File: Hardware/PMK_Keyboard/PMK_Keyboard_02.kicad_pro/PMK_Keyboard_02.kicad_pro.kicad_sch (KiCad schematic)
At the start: 0 parts

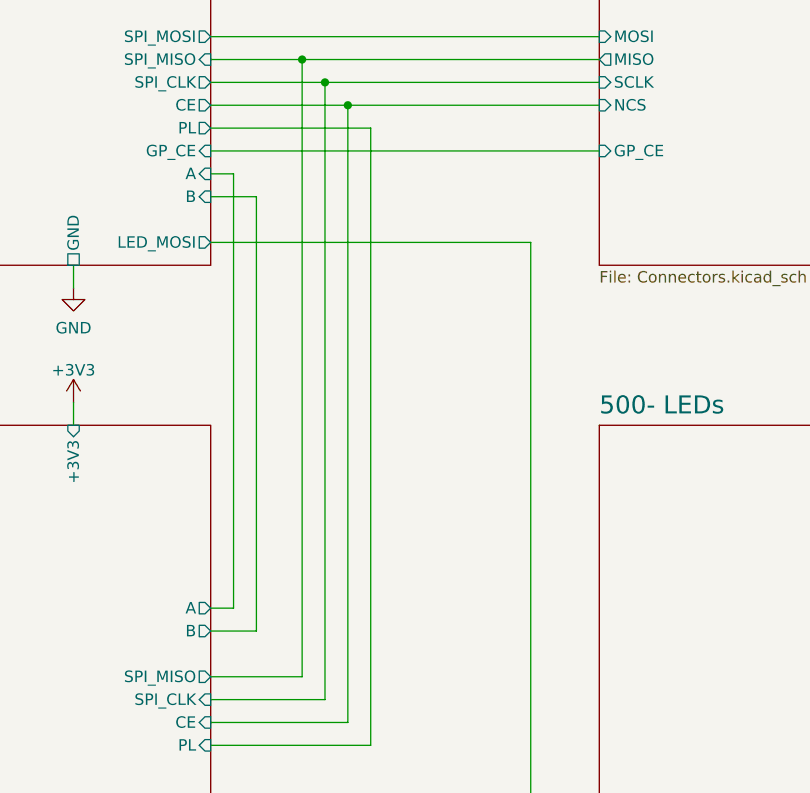
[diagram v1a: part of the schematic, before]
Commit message: added module connector
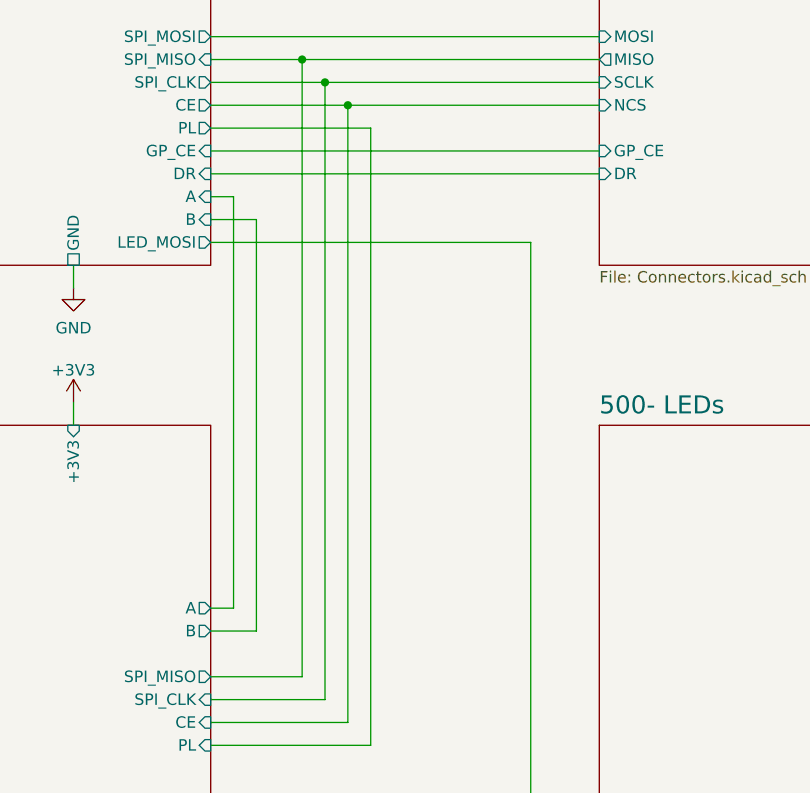
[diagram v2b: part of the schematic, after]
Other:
- sheet 200- PSoM ports: added DR; removed none
- sheet 300- Connectors ports: added DR; removed none
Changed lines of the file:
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@@
 	(wire
 		(pts
-			(xy 124.46 124.46) (xy 124.46 76.2)
+			(xy 124.46 124.46) (xy 124.46 78.74)
 		)
 		(stroke
@@
 	(wire
 		(pts
-			(xy 119.38 73.66) (xy 121.92 73.66)
+			(xy 119.38 76.2) (xy 121.92 76.2)
 		)
 		(stroke
@@
 	(wire
 		(pts
-			(xy 121.92 73.66) (xy 121.92 121.92)
+			(xy 121.92 76.2) (xy 121.92 121.92)
 		)
 		(stroke
@@
 	(wire
 		(pts
+			(xy 119.38 73.66) (xy 162.56 73.66)
+		)
+		(stroke
+			(width 0)
+			(type default)
+		)
+	)
+	(wire
+		(pts
 			(xy 215.9 30.48) (xy 215.9 33.02)
 		)
@@
 	(wire
 		(pts
-			(xy 124.46 76.2) (xy 119.38 76.2)
+			(xy 124.46 78.74) (xy 119.38 78.74)
 		)
 		(stroke
@@
 			)
 		)
+		(pin "DR" input
+			(at 162.56 73.66 180)
+			(effects
+				(font
+					(size 1.27 1.27)
+				)
+				(justify left)
+			)
+		)
 		(instances
 			(project "PMK_Keyboard_02.kicad_pro"
@@
 		)
 		(pin "B" input
+			(at 119.38 78.74 0)
+			(effects
+				(font
+					(size 1.27 1.27)
+				)
+				(justify right)
+			)
+		)
+		(pin "A" input
 			(at 119.38 76.2 0)
-			(effects
-				(font
-					(size 1.27 1.27)
-				)
-				(justify right)
-			)
-		)
-		(pin "A" input
-			(at 119.38 73.66 0)
 			(effects
 				(font
@@
 			(effects
 				(font
+					(size 1.27 1.27)
+				)
+				(justify right)
+			)
+		)
+		(pin "DR" input
+			(at 119.38 73.66 0)
+			(effects
+				(font

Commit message: working on routing
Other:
- sheet 400- Shift Register - Switch ports: added DB_A, DB_B; removed A, B
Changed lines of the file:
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@@
 			)
 		)
-		(pin "B" output
-			(at 119.38 124.46 0)
+		(pin "DB_A" output
+			(at 119.38 121.92 0)
 			(effects
 				(font
@@
 			)
 		)
-		(pin "A" output
-			(at 119.38 121.92 0)
+		(pin "DB_B" output
+			(at 119.38 124.46 0)
 			(effects
 				(font

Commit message: routing ongoing
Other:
- sheet 200- PSoM ports: added DB_A, DB_B, GPIO1, GPIO2, GPIO3, SR_CE; removed A, B, CE, INT
- sheet 300- Connectors ports: added GPIO1, GPIO2, GPIO3; removed INT, NCS
